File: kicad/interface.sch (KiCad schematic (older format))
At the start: 37 parts, among them P10 C3SB, P11 VSel_Vlv, P14 X_VALVE, P17 PUMP, P18 Pump_Cable, P34 VSel_Vlv2, P38 X_VALVE2, P7 GAGE_PR, P9 C3SB, Q1 BCP5416TA, Q2 BCP5416TA, Q3 BCP5416TA, Q4 BCP5416TA, U1 TXB0104D

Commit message: made a pretty schematic, fresh symbols
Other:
- note added: "HCEM500GUH9P3 = 3V device\nHCEM500GUH9P5 = 5V device\nIf using HCE...5, \nDNP U1, R4, R7\nand Short U1 pins\n1<>14,\n2<>13,\n3<>12, \n4<>11, 5<>10"
- note added: "Pump, 12V DC [P54E01R], PWM"
- note added: "Speaker, PWM"
- note added: "Valve #1, Digital port PD4, 12V (V_IN) or 5V0"
- note added: "Valve #2, Digital port PD5 [PWM], 12V (V_IN) or 5V0"
- note removed: "If using HCE...5, \nDNP U1, R4, R7\nand Short U1 pins\n1<>14, 2<>13, 3<>12, \n4<>11, 5<>10"
- note removed: "Pump, 12V DC [P54E01R]\non digital port ~PB1"
- note removed: "Speaker, 5V DC\ndigital PWM port ~PD6"
- note removed: "Valve #1 on digital port PD4\neither 12V (V_IN) or 5V0"
- note removed: "Valve #2 on digital port PD5 [PWM]\neither 12V (V_IN) or 5V0"

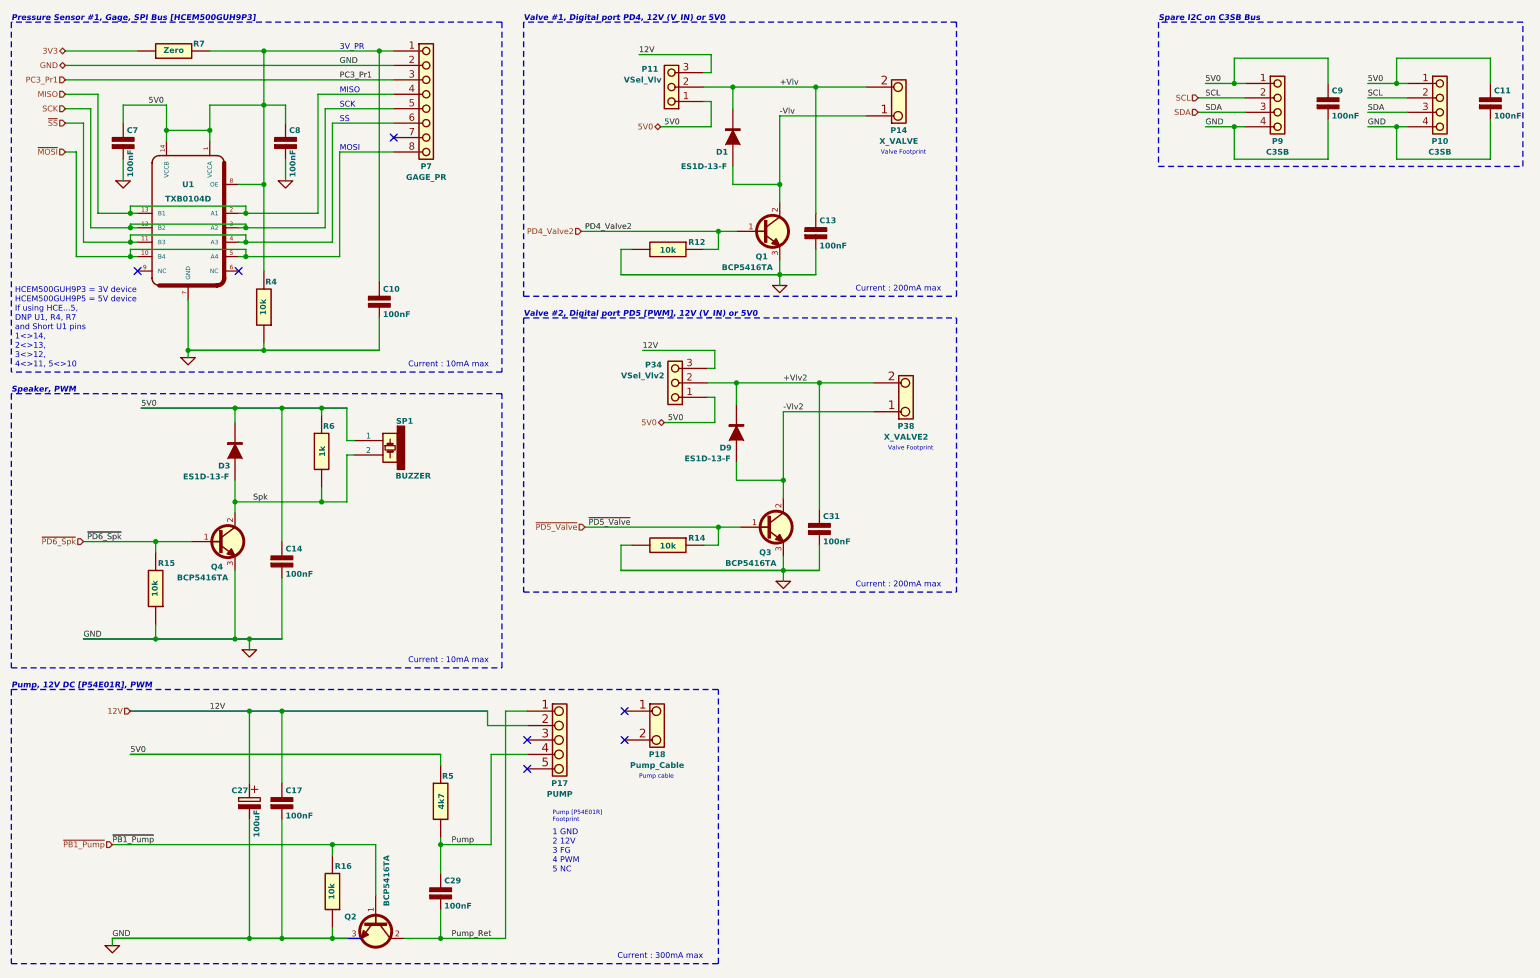
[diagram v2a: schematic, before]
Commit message: schematic label errors corrected, Git issue #2
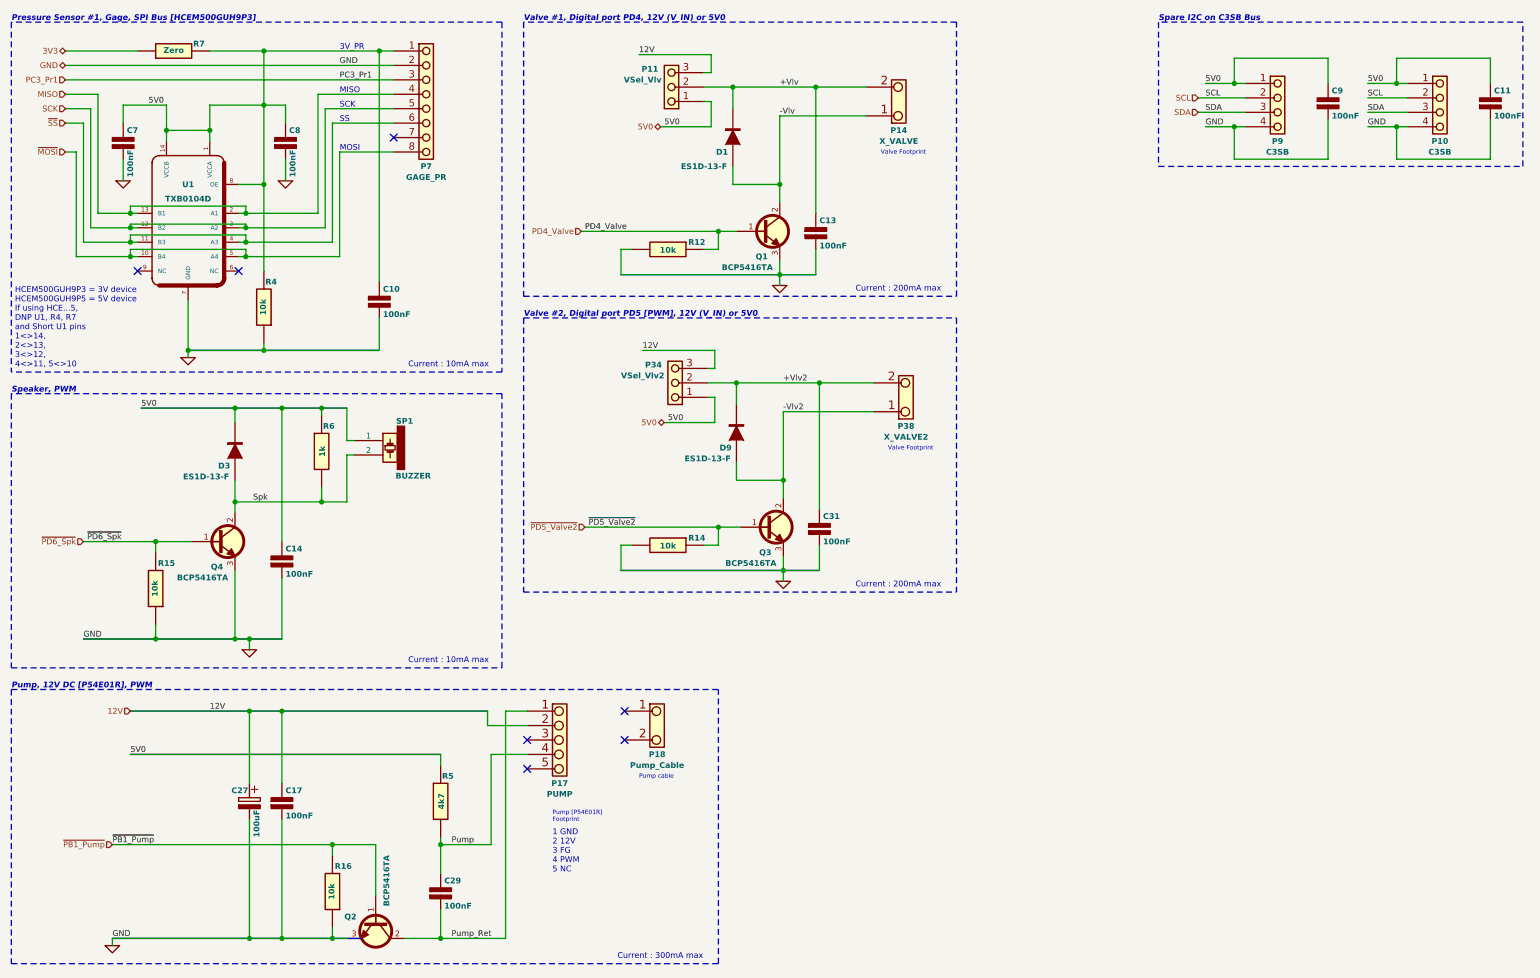
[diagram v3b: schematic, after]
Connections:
- net PD4_Valve2 renamed PD4_Valve
- net ~PD5_Valve renamed ~PD5_Valve2
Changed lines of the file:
@@
 Connection ~ 5675 1025
 Wire Wire Line
-	5475 1025 5675 1025
-Wire Wire Line
-	5675 1025 6250 1025
-Wire Wire Line
-	6250 1025 6600 1025
+	5475 1025 6600 1025
 Wire Notes Line
 	675  575  675  3000
@@
 	8900 1200 9225 1200
 Wire Wire Line
-	8950 1000 9150 1000
-Wire Wire Line
-	9150 1000 9225 1000
+	8950 1000 9225 1000
 Connection ~ 1900 2850
 Wire Wire Line
@@
 	2575 1150 2575 1275
 Wire Wire Line
-	2050 1150 2425 1150
-Wire Wire Line
-	2425 1150 2575 1150
-Wire Wire Line
-	1900 2500 1900 2850
-Wire Wire Line
-	1900 2850 1900 2900
+	2050 1150 2575 1150
+Wire Wire Line
+	1900 2500 1900 2900
 Wire Wire Line
 	1050 1275 1175 1275
@@
 	1175 1275 1175 2100
 Wire Wire Line
-	1175 2100 1500 2100
-Wire Wire Line
-	1500 2100 1550 2100
+	1175 2100 1550 2100
 Wire Wire Line
 	1050 1075 1275 1075
@@
 	1275 1075 1275 1900
 Wire Wire Line
-	1275 1900 1500 1900
-Wire Wire Line
-	1500 1900 1550 1900
-Wire Wire Line
-	2250 2000 2300 2000
-Wire Wire Line
-	2300 2000 2850 2000
+	1275 1900 1550 1900
+Wire Wire Line
+	2250 2000 2850 2000
 Wire Wire Line
 	2850 2000 2850 1175
@@
 	2850 1175 3325 1175
 Wire Wire Line
-	2250 2200 2300 2200
-Wire Wire Line
-	2300 2200 2950 2200
+	2250 2200 2950 2200
 Wire Wire Line
 	2950 2200 2950 1475
 Wire Wire Line
-	1375 6925 2325 6925
-Wire Wire Line
-	2325 6925 2550 6925
-Wire Wire Line
-	2550 6925 2900 6925
-Wire Wire Line
-	2900 6925 3000 6925
-Wire Wire Line
-	3400 6925 3650 6925
-Wire Wire Line
-	3650 6925 4100 6925
+	1375 6925 3000 6925
+Wire Wire Line
+	3400 6925 4100 6925
 Wire Wire Line
 	5025 800  5525 800
@@
 	5675 1575 5675 1700
 Wire Wire Line
-	6000 2225 6000 2325
-Wire Wire Line
-	6000 2325 6000 2400
-Wire Wire Line
-	6000 1225 6000 1700
-Wire Wire Line
-	6000 1700 6000 1825
+	6000 2225 6000 2400
+Wire Wire Line
+	6000 1225 6000 1825
 Wire Wire Line
 	2950 1475 3325 1475
@@
 	1050 975  3325 975
 Wire Wire Line
-	4625 2025 5575 2025
-Wire Wire Line
-	5575 2025 5700 2025
+	4625 2025 5700 2025
 Wire Wire Line
 	3650 6725 3650 6925
@@
 	6250 2325 6250 2150
 Wire Wire Line
-	4900 2325 6000 2325
-Wire Wire Line
-	6000 2325 6250 2325
+	4900 2325 6250 2325
 Connection ~ 6000 2325
 Wire Wire Line
@@
 	2900 1275 2900 2100
 Wire Wire Line
-	2900 2100 2300 2100
-Wire Wire Line
-	2300 2100 2250 2100
+	2900 2100 2250 2100
 Wire Wire Line
 	3325 1075 2800 1075
@@
 	2800 1075 2800 1900
 Wire Wire Line
-	2800 1900 2300 1900
-Wire Wire Line
-	2300 1900 2250 1900
-Wire Wire Line
-	1225 2000 1500 2000
-Wire Wire Line
-	1500 2000 1550 2000
+	2800 1900 2250 1900
+Wire Wire Line
+	1225 2000 1550 2000
 Wire Wire Line
 	1225 2000 1225 1175
@@
 	1225 1175 1050 1175
 Wire Wire Line
-	1125 2200 1500 2200
-Wire Wire Line
-	1500 2200 1550 2200
+	1125 2200 1550 2200
 Wire Wire Line
 	1125 2200 1125 1475
@@
 	1125 1475 1050 1475
 Wire Wire Line
-	2050 1150 2050 1325
-Wire Wire Line
-	2050 1325 2050 1400
-Wire Wire Line
-	1750 1150 1750 1325
-Wire Wire Line
-	1750 1325 1750 1400
+	2050 1150 2050 1400
+Wire Wire Line
+	1750 1150 1750 1400
 Wire Wire Line
 	2575 1525 2575 1675
@@
 	1450 1525 1450 1675
 Wire Wire Line
-	2425 775  2425 1150
-Wire Wire Line
-	2425 1150 2425 1700
-Wire Wire Line
-	2425 1700 2425 2300
+	2425 775  2425 2300
 Connection ~ 2425 1700
 Wire Notes Line
@@
 	8900 1100 9225 1100
 Wire Wire Line
-	8950 1300 9150 1300
-Wire Wire Line
-	9150 1300 9225 1300
+	8950 1300 9225 1300
 Wire Wire Line
 	9150 1300 9150 1525
@@
 	3225 2850 3225 2625
 Wire Wire Line
-	1900 2850 2425 2850
-Wire Wire Line
-	2425 2850 3225 2850
+	1900 2850 3225 2850
 Connection ~ 2425 2850
 Wire Notes Line
@@
 	10275 1525 10275 1300
 Wire Wire Line
-	10075 1300 10275 1300
-Wire Wire Line
-	10275 1300 10350 1300
+	10075 1300 10350 1300
 Wire Wire Line
 	10075 1100 10350 1100
 Wire Wire Line
-	10075 1000 10275 1000
-Wire Wire Line
-	10275 1000 10350 1000
+	10075 1000 10350 1000
 Wire Wire Line
 	10075 1200 10350 1200
@@
 $EndComp
 Text HLabel 4650 4075 0    40   Input ~ 0
-~PD5_Valve
+~PD5_Valve2
 Text HLabel 1500 5350 0    40   Input ~ 0
 12V
@@
 3V3
 Text Label 4675 4075 0    40   ~ 0
-~PD5_Valve
+~PD5_Valve2
 Text Notes 4225 575  0    40   Italic 8
 Valve #1, Digital port PD4, 12V (V_IN) or 5V0
@@
 $EndComp
 Wire Wire Line
-	1500 5350 2325 5350
-Wire Wire Line
-	2325 5350 2550 5350
-Wire Wire Line
-	2550 5350 3975 5350
-Wire Wire Line
-	1375 6275 2900 6275
-Wire Wire Line
-	2900 6275 3200 6275
+	1500 5350 3975 5350
+Wire Wire Line
+	1375 6275 3200 6275
 $Comp
 L CONN_2 P18
@@
 	4000 6275 3650 6275
 Wire Wire Line
-	3650 6225 3650 6275
-Wire Wire Line
-	3650 6275 3650 6475
+	3650 6225 3650 6475
 Wire Wire Line
 	3650 5650 3650 5725
@@
 Connection ~ 5700 3075
 Wire Wire Line
-	5500 3075 5700 3075
-Wire Wire Line
-	5700 3075 6275 3075
-Wire Wire Line
-	6275 3075 6650 3075
+	5500 3075 6650 3075
 Wire Wire Line
 	5050 2850 5550 2850
@@
 	5700 3625 5700 3750
 Wire Wire Line
-	6025 4275 6025 4375
-Wire Wire Line
-	6025 4375 6025 4450
-Wire Wire Line
-	6025 3275 6025 3750
-Wire Wire Line
-	6025 3750 6025 3875
-Wire Wire Line
-	4650 4075 5575 4075
-Wire Wire Line
-	5575 4075 5725 4075
+	6025 4275 6025 4450
+Wire Wire Line
+	6025 3275 6025 3875
+Wire Wire Line
+	4650 4075 5725 4075
 Wire Wire Line
 	5700 3225 5700 3075
@@
 	6275 4375 6275 4200
 Wire Wire Line
-	4900 4375 6025 4375
-Wire Wire Line
-	6025 4375 6275 4375
+	4900 4375 6275 4375
 Connection ~ 6025 4375
 Wire Notes Line
@@
 $EndComp
 Text HLabel 4625 2025 0    40   Input ~ 0
-PD4_Valve2
+PD4_Valve
 Text Label 4650 2025 0    40   ~ 0
-PD4_Valve2
+PD4_Valve
 Text Notes 4225 2625 0    40   Italic 8
 Valve #2, Digital port PD5 [PWM], 12V (V_IN) or 5V0
@@
 	2550 4850 2550 4425
 Wire Wire Line
-	1175 4850 1675 4850
-Wire Wire Line
-	1675 4850 2225 4850
-Wire Wire Line
-	2225 4850 2325 4850
-Wire Wire Line
-	2325 4850 2550 4850
+	1175 4850 2550 4850
 Connection ~ 2325 4850
 Wire Wire Line
@@
 Connection ~ 2225 3250
 Wire Wire Line
-	2225 3750 2225 3900
-Wire Wire Line
-	2225 3900 2225 3975
+	2225 3750 2225 3975
 Wire Wire Line
 	2225 4375 2225 4850
 Connection ~ 2225 4850
 Wire Wire Line
-	1575 3250 2225 3250
-Wire Wire Line
-	2225 3250 2550 3250
-Wire Wire Line
-	2550 3250 2825 3250
-Wire Wire Line
-	2825 3250 3000 3250
+	1575 3250 3000 3250
 Wire Wire Line
 	2550 3250 2550 4175
 Wire Wire Line
-	1175 4175 1675 4175
-Wire Wire Line
-	1675 4175 1925 4175
+	1175 4175 1925 4175
 Text Label 1200 4175 0    40   ~ 0
 ~PD6_Spk
@@
 	2825 3800 2825 3900
 Wire Wire Line
-	2225 3900 2825 3900
-Wire Wire Line
-	2825 3900 3000 3900
+	2225 3900 3000 3900
 Wire Wire Line
 	3000 3900 3000 3575
@@
 Current : 200mA max
 Wire Wire Line
-	2050 775  2425 775
-Wire Wire Line
-	2425 775  3225 775
-Wire Wire Line
-	3225 775  3325 775
+	2050 775  3325 775
 $Comp
 L R R7
@@
 Connection ~ 2325 6925
 Wire Bus Line
-	4900 2325 6000 2325
+	4900 2325 6250 2325
 Wire Bus Line
-	6000 2325 6250 2325
+	4900 4375 6275 4375
 Wire Bus Line
-	4900 4375 6025 4375
+	1375 6925 3100 6925
 Wire Bus Line
-	6025 4375 6275 4375
-Wire Bus Line
-	1375 6925 2325 6925
-Wire Bus Line
-	2325 6925 2550 6925
-Wire Bus Line
-	2550 6925 2900 6925
-Wire Bus Line
-	2900 6925 3100 6925
-Wire Bus Line
-	1500 5350 2325 5350
-Wire Bus Line
-	2325 5350 2550 5350
-Wire Bus Line
-	2550 5350 3975 5350
+	1500 5350 3975 5350
 Wire Bus Line
 	1500 5650 3650 5650
 Wire Bus Line
-	1175 4850 1675 4850
+	1175 4850 2550 4850
 Wire Bus Line
-	1675 4850 2225 4850
+	1575 3250 3000 3250
 Wire Bus Line
-	2225 4850 2325 4850
-Wire Bus Line
-	2325 4850 2550 4850
-Wire Bus Line
-	1575 3250 2225 3250
-Wire Bus Line
-	2225 3250 2550 3250
-Wire Bus Line
-	2550 3250 2825 3250
-Wire Bus Line
-	2825 3250 3000 3250
-Wire Bus Line
-	1900 2850 2425 2850
-Wire Bus Line
-	2425 2850 3225 2850
+	1900 2850 3225 2850
 $EndSCHEMATC
